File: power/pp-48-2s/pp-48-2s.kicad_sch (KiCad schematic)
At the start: 174 parts, among them J1 BUS 40-60V, J101 NODE 1, J2 CTRL IN, J201 NODE 2, J3 CTRL OUT, J4 12V AUX OUT, J5 SWD, Q1 2N7002, Q101 BSC070N10NS5, Q102 2N7002, Q103 2N7002, Q104 2N7002, Q201 BSC070N10NS5, Q202 2N7002, Q203 2N7002, Q204 2N7002, U1 LM5164DDA, U101 LM5069MM-2, U102 INA238AIDGSR, U103 74LVC1G74, U104 TLP176AM, U105 TLP176AM, U106 TLP291, U2 LM5164DDA, U201 LM5069MM-2, U202 INA238AIDGSR, U203 74LVC1G74, U204 TLP176AM, U205 TLP176AM, U206 TLP291, U3 STM32G0B1CBT6, U4 ISO1640BD, U5 ISO7721D, U6 MCP23017-E/SO, X101 PM-19V-200W, X102 J2 AUX, X201 PM-19V-200W, X202 J2 AUX, Y1 8MHz

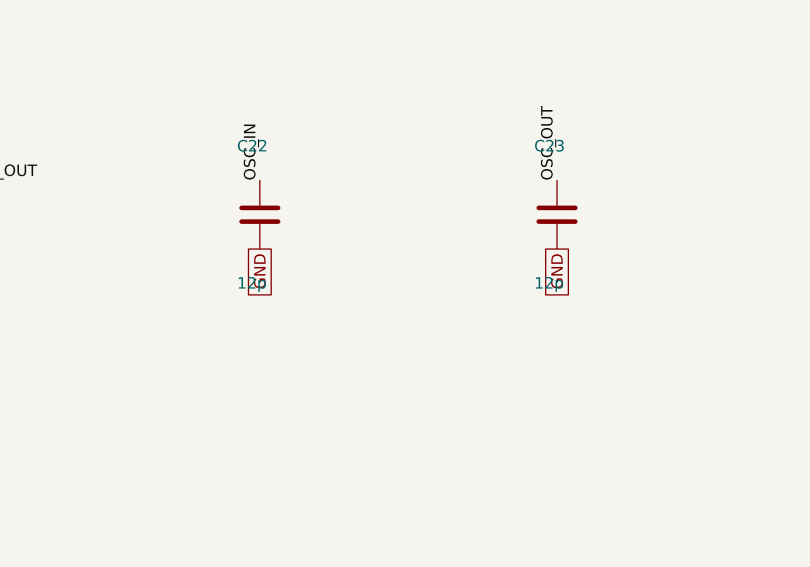
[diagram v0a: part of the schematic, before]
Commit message: power: PP-48-2S WIP checkpoint: placed, power copper, gndpour, KRT routed
tools/place.py (sockets, node connectors, bus terminal, MCU corner),
tools/power.py (VBUS trunk/artery/bar on B.Cu, slot SENSE/OUT/NODE,
GND stubs for fine-pitch pads, GND zones into the kept group),
tools/syncfields.py; gensch.py fills LCSC numbers (116 of 174).
Outline 150 x 95 mm, clearance 0.15 mm, KRT with --ordering mps
--no-stub-layer-swap. DRC: 4 unconnected (+3V3 C203, /FB2 C13,
/S1_ID U3, /S1_LQ U103), 2 clearance (S1_OUT/S1_PGD 0.149 mm),
3 starved thermals, silk untouched. Netlist pp-48-2s.xml matches
the schematic.
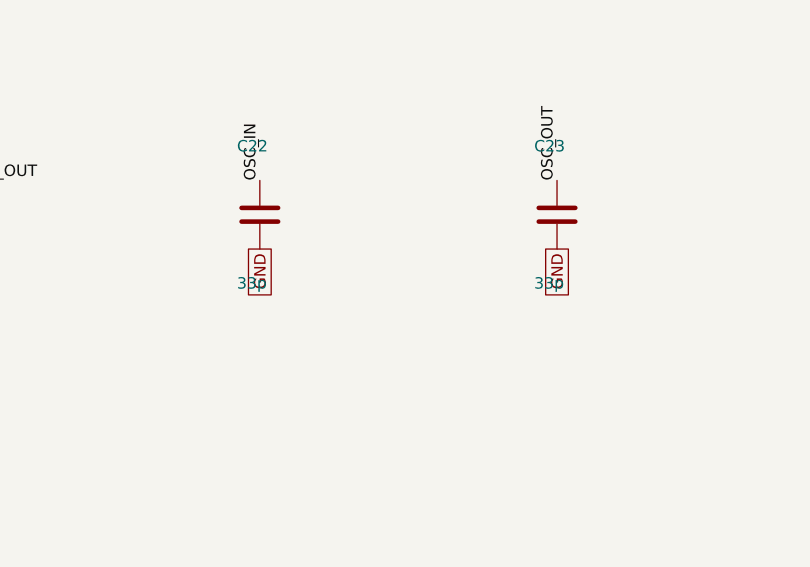
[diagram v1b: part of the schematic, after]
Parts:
- C1, C102, C14, C2, C202, C7: LCSC (none) -> C338133
- C103, C104, C105, C106, C107, C13, C18, C20, C203, C204, C205, C206, C207, C21, C24, C25, C26, C27, C28, C6: LCSC (none) -> C1525
- C22, C23: value 12p -> 33p
- J101, J201: MPN (none) -> Molex 39-28-1083
- J2, J3: LCSC (none) -> C157993
- J4: LCSC (none) -> C131337
- L1: LCSC (none) -> C840528; MPN (none) -> Bourns SRR1260-330M
- L2: MPN (none) -> Bourns SRR1260-680M
- R101, R102, R201, R202: LCSC (none) -> C2904232
- R104, R106, R108, R113, R114, R115, R116, R204, R206, R208, R213, R214, R215, R216, R25: LCSC (none) -> C25744
- R109, R11, R110, R111, R112, R15, R20, R209, R21, R210, R211, R212, R22, R30: LCSC (none) -> C25741
- R118, R218: LCSC (none) -> C25804
- R121, R221: LCSC (none) -> C25091
- R122, R222: LCSC (none) -> C25792
- R18, R19: LCSC (none) -> C11702
- R23, R24: LCSC (none) -> C25879
- R26, R27, R28, R29: LCSC (none) -> C25900
- U1, U2: LCSC (none) -> C477928
- U103, U203: LCSC (none) -> C70285
- U104, U105, U204, U205: LCSC (none) -> C5370540
- U106, U206: LCSC (none) -> C55144
- U3: LCSC (none) -> C2847904
- U4: LCSC (none) -> C5122339
- U5: LCSC (none) -> C366164
- U6: LCSC (none) -> C47023
- Y1: LCSC (none) -> C7424755

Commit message: power: PP-48-2S schematic regenerated as drawn hierarchical sheets (ADR 0002)
tools/gensch.py now writes a root sheet and sheets/{input,bucks,mcu,link,
expanders,slot}.kicad_sch from the drawing engine in tools/sch (blocks
in tools/sch/blocks); the slot is one file instantiated per slot.
ERC 0 (--severity-all). tools/schcheck.py: every (ref, pin) -> net
identical to the previous flat netlist, 71 nets renamed to sheet-path
names, 4 expected field differences (shared slot sheet). Board relinked
with pcbkit relink: 174 paths, 71 nets, DRC unchanged (0 unconnected,
4 starved_thermal, 1 silk_edge). power.py and the handroute plans carry
the new net names. Regenerate twice is byte identical.
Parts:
- removed C1, C102, C14, C2, C202, C7: 2.2u 100V, Capacitor_SMD:C_1210_3225Metric, symbol Device:C
- removed C10, C9: 22u 10V, Capacitor_SMD:C_1210_3225Metric, symbol Device:C
- removed C101, C201: 220n, Capacitor_SMD:C_0603_1608Metric, symbol Device:C
- removed C103, C104, C105, C106, C107, C13, C18, C20, C203, C204, C205, C206, C207, C21, C24, C25, C26, C27, C28, C6: 100n, Capacitor_SMD:C_0402_1005Metric, symbol Device:C
- removed C108, C208: 2.2u 50V, Capacitor_SMD:C_1210_3225Metric, symbol Device:C
- removed C11, C4: 2.2n 50V, Capacitor_SMD:C_0402_1005Metric, symbol Device:C
- removed C12: 2.2n, Capacitor_SMD:C_0402_1005Metric, symbol Device:C
- removed C15, C8: 100n 100V, Capacitor_SMD:C_0603_1608Metric, symbol Device:C
- removed C16, C17: 22u 25V, Capacitor_SMD:C_1210_3225Metric, symbol Device:C
- removed C19: 4.7u, Capacitor_SMD:C_0603_1608Metric, symbol Device:C
- removed C22, C23: 33p, Capacitor_SMD:C_0402_1005Metric, symbol Device:C
- removed C3: 10n, Capacitor_SMD:C_0402_1005Metric, symbol Device:C
- removed C5: 1.5n, Capacitor_SMD:C_0402_1005Metric, symbol Device:C
- removed D1, D101, D201: SMBJ60A, Diode_SMD:D_SMB, symbol Device:D_TVS
- removed D102, D202: GREEN ON, LED_SMD:LED_0603_1608Metric, symbol Device:LED
- removed D103, D203: GREEN NODE, LED_SMD:LED_0603_1608Metric, symbol Device:LED
- removed D2: GREEN 12V, LED_SMD:LED_0603_1608Metric, symbol Device:LED
- removed D3: GREEN 3V3, LED_SMD:LED_0603_1608Metric, symbol Device:LED
- removed D4: GREEN RUN, LED_SMD:LED_0603_1608Metric, symbol Device:LED
- removed F1: 10A nano2, Fuse:Fuse_Littelfuse-NANO2-451_453, symbol Device:Fuse
- removed F2: 1.5A, Fuse:Fuse_1206_3216Metric, symbol Device:Fuse
- removed J1: BUS 40-60V, TerminalBlock_Phoenix:TerminalBlock_Phoenix_MKDS-3-2-5.08_1x02_P5.08mm_Horizontal, symbol Connector:Screw_Terminal_01x02
- removed J101: NODE 1, Connector_Molex:Molex_Mini-Fit_Jr_5566-08A_2x04_P4.20mm_Vertical, symbol Connector_Generic:Conn_02x04_Odd_Even
- removed J2: CTRL IN, Connector_JST:JST_PH_B5B-PH-K_1x05_P2.00mm_Vertical, symbol Connector_Generic:Conn_01x05
- removed J201: NODE 2, Connector_Molex:Molex_Mini-Fit_Jr_5566-08A_2x04_P4.20mm_Vertical, symbol Connector_Generic:Conn_02x04_Odd_Even
- removed J3: CTRL OUT, Connector_JST:JST_PH_B5B-PH-K_1x05_P2.00mm_Vertical, symbol Connector_Generic:Conn_01x05
- removed J4: 12V AUX OUT, Connector_JST:JST_PH_B2B-PH-K_1x02_P2.00mm_Vertical, symbol Connector_Generic:Conn_01x02
- removed J5: SWD, Connector:Tag-Connect_TC2030-IDC-NL_2x03_P1.27mm_Vertical, symbol Connector:Conn_ARM_SWD_TagConnect_TC2030-NL
- removed JP1: ADR0, Jumper:SolderJumper-2_P1.3mm_Open_RoundedPad1.0x1.5mm, symbol Jumper:SolderJumper_2_Open
- removed JP2: ADR1, Jumper:SolderJumper-2_P1.3mm_Open_RoundedPad1.0x1.5mm, symbol Jumper:SolderJumper_2_Open
- removed JP3: ADR2, Jumper:SolderJumper-2_P1.3mm_Open_RoundedPad1.0x1.5mm, symbol Jumper:SolderJumper_2_Open
- removed L1: 33u, Inductor_SMD:L_12x12mm_H6mm, symbol Device:L
- removed L2: 68u, Inductor_SMD:L_12x12mm_H6mm, symbol Device:L
- removed Q1, Q102, Q103, Q104, Q202, Q203, Q204: 2N7002, Package_TO_SOT_SMD:SOT-23, symbol Transistor_FET:2N7002
- removed Q101, Q201: BSC070N10NS5, Package_TO_SOT_SMD:TDSON-8-1, symbol Transistor_FET:BSC070N10NS5
- removed R1: 470k, Resistor_SMD:R_0805_2012Metric, symbol Device:R
- removed R10, R4: 52.3k, Resistor_SMD:R_0402_1005Metric, symbol Device:R
- removed R101, R102, R201, R202: 7m 2W, Resistor_SMD:R_2512_6332Metric, symbol Device:R
- removed R103, R203: 143k, Resistor_SMD:R_0805_2012Metric, symbol Device:R
- removed R104, R106, R108, R113, R114, R115, R116, R204, R206, R208, R213, R214, R215, R216, R25: 10k, Resistor_SMD:R_0402_1005Metric, symbol Device:R
- removed R105, R205: 240k, Resistor_SMD:R_0805_2012Metric, symbol Device:R
- removed R107, R207: 13.7k, Resistor_SMD:R_0402_1005Metric, symbol Device:R
- removed R109, R11, R110, R111, R112, R15, R20, R209, R21, R210, R211, R212, R22, R30: 100k, Resistor_SMD:R_0402_1005Metric, symbol Device:R
- removed R117, R217: 47k, Resistor_SMD:R_1206_3216Metric, symbol Device:R
- removed R118, R218: 10k, Resistor_SMD:R_0603_1608Metric, symbol Device:R
- removed R119, R120, R219, R220: 270, Resistor_SMD:R_0402_1005Metric, symbol Device:R
- removed R12, R14, R8: 453k, Resistor_SMD:R_0402_1005Metric, symbol Device:R
- removed R121, R221: 220, Resistor_SMD:R_0402_1005Metric, symbol Device:R
- removed R122, R222: 47k, Resistor_SMD:R_0402_1005Metric, symbol Device:R
- removed R13, R7: 49.9k, Resistor_SMD:R_0402_1005Metric, symbol Device:R
- removed R16: 27k, Resistor_SMD:R_0402_1005Metric, symbol Device:R
- removed R17: 4.7k, Resistor_SMD:R_0603_1608Metric, symbol Device:R
- removed R18, R19: 1k, Resistor_SMD:R_0402_1005Metric, symbol Device:R
- removed R2: 13k, Resistor_SMD:R_0402_1005Metric, symbol Device:R
- removed R23, R24: 2.2k, Resistor_SMD:R_0402_1005Metric, symbol Device:R
- removed R26, R27, R28, R29: 4.7k, Resistor_SMD:R_0402_1005Metric, symbol Device:R
- removed R3, R9: 1M, Resistor_SMD:R_0805_2012Metric, symbol Device:R
- removed R5: 41.2k, Resistor_SMD:R_0402_1005Metric, symbol Device:R
- removed R6: 86.6k, Resistor_SMD:R_0402_1005Metric, symbol Device:R
- removed U1, U2: LM5164DDA, Package_SO:HSOP-8-1EP_3.9x4.9mm_P1.27mm_EP2.41x3.1mm, symbol Regulator_Switching:LM5164DDA
- removed U101, U201: LM5069MM-2, Package_SO:MSOP-10_3x3mm_P0.5mm, symbol Power_Management:LM5069MM-2
- removed U102, U202: INA238AIDGSR, Package_SO:TSSOP-10_3x3mm_P0.5mm, symbol Sensor_Energy:INA238
- removed U103, U203: 74LVC1G74, Package_SO:VSSOP-8_2.3x2mm_P0.5mm, symbol 74xGxx:74AUC1G74
- removed U104, U105, U204, U205: TLP176AM, Package_SO:SOIC-4_4.55x3.7mm_P2.54mm, symbol pp:TLP176AM
- removed U106, U206: TLP291, Package_SO:SOIC-4_4.55x2.6mm_P1.27mm, symbol Isolator:TLP291
- removed U3: STM32G0B1CBT6, Package_QFP:LQFP-48_7x7mm_P0.5mm, symbol MCU_ST_STM32G0:STM32G0B1CBTx
- removed U4: ISO1640BD, Package_SO:SOIC-8_3.9x4.9mm_P1.27mm, symbol Isolator:ISO1540
- removed U5: ISO7721D, Package_SO:SOIC-8_3.9x4.9mm_P1.27mm, symbol Isolator:ISO7721D
- removed U6: MCP23017-E/SO, Package_SO:SOIC-28W_7.5x17.9mm_P1.27mm, symbol Interface_Expansion:MCP23017x-x-SO
- removed X101, X201: PM-19V-200W, pp:Brick_Eighth_DOSA_Plane, symbol pp:PM_Brick_Socket
- removed X102, X202: J2 AUX, Connector_PinHeader_1.27mm:PinHeader_1x07_P1.27mm_Vertical, symbol Connector_Generic:Conn_01x07
- removed Y1: 8MHz, Crystal:Crystal_SMD_3225-4Pin_3.2x2.5mm, symbol Device:Crystal_GND24
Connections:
- no-connect marks 42 -> 0
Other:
- added sheet Bucks (sheets/bucks.kicad_sch)
- added sheet Expanders (sheets/expanders.kicad_sch)
- added sheet Input (sheets/input.kicad_sch)
- added sheet Link (sheets/link.kicad_sch)
- added sheet MCU (sheets/mcu.kicad_sch)
- added sheet Slot 1 (sheets/slot.kicad_sch)
- added sheet Slot 2 (sheets/slot.kicad_sch)
- note added: "INA238 address pins A1 (pin 1) and A0 (pin 2) tied per slot at the slot sheet pins: address 0x40 + slot - 1"
- note added: "POWER ANCHORS"
- note removed: "CORE: input, 3V3 and 12 V aux bucks (LM5164), STM32G0B1, isolators, controller link"
- note removed: "POWER ANCHORS (power symbols joined to the net labels)"
- note removed: "SLOT 1: LM5069-2 + INA238 on 3.5 mOhm, OV latch, brick socket, node connector (PWR/RST/LED)"
- note removed: "SLOT 2: LM5069-2 + INA238 on 3.5 mOhm, OV latch, brick socket, node connector (PWR/RST/LED)"
